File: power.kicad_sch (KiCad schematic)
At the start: 36 parts, among them J501 PJ-002AH-SMT-TR, Q501 DMG2307LQ, U501 LMR50410, U502 TLV1117-50, U503 TLV74133PDBVR

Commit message: Update some part numbers for in-stock parts
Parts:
- C501, C505, C511, C512: footprint Capacitor_SMD:CP_Elec_6.3x7.7 -> Capacitor_SMD:CP_Elec_6.3x5.8; PN EEEFK1E101XP -> EEEFK1E101SP
- D502: value TZMC12-GS08 -> TZMC10-GS08; PN TZMC12-GS08 -> TZMC10-GS08
- FB501, FB502, FB503: value 600R@100MHz -> 1000R@100MHz; PN BLM21SP601SN1 -> 2508051027Y1
- Q501: value DMG2307LQ -> SI2371EDS-T1-GE3; PN DMG2307LQ -> SI2371EDS-T1-GE3
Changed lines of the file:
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@@
       (effects (font (size 1.27 1.27)) (justify left))
     )
-    (property "Value" "TZMC12-GS08" (id 1) (at 88.9 36.8299 90)
+    (property "Value" "TZMC10-GS08" (id 1) (at 88.9 36.8299 90)
       (effects (font (size 1.27 1.27)) (justify left))
     )
@@
       (effects (font (size 1.27 1.27)) hide)
     )
-    (property "PN" "TZMC12-GS08" (id 4) (at 86.36 35.56 0)
+    (property "PN" "TZMC10-GS08" (id 4) (at 86.36 35.56 0)
       (effects (font (size 1.27 1.27)) hide)
     )
@@
       (effects (font (size 1.27 1.27)) (justify left))
     )
-    (property "Footprint" "Capacitor_SMD:CP_Elec_6.3x7.7" (id 2) (at 111.76 45.72 0)
-      (effects (font (size 1.27 1.27)) hide)
-    )
-    (property "Datasheet" "https://industrial.panasonic.com/cdbs/www-data/pdf/RDE0000/ABA0000C1181.pdf" (id 3) (at 111.76 45.72 0)
-      (effects (font (size 1.27 1.27)) hide)
-    )
-    (property "PN" "EEEFK1E101XP" (id 4) (at 111.76 45.72 0)
+    (property "Footprint" "Capacitor_SMD:CP_Elec_6.3x5.8" (id 2) (at 111.76 45.72 0)
+      (effects (font (size 1.27 1.27)) hide)
+    )
+    (property "Datasheet" "https://www.mouser.co.uk/datasheet/2/315/ABA0000C1251-1138508.pdf" (id 3) (at 111.76 45.72 0)
+      (effects (font (size 1.27 1.27)) hide)
+    )
+    (property "PN" "EEEFK1E101SP" (id 4) (at 111.76 45.72 0)
       (effects (font (size 1.27 1.27)) hide)
     )
@@
       (effects (font (size 1.27 1.27)) (justify left))
     )
-    (property "Footprint" "Capacitor_SMD:CP_Elec_6.3x7.7" (id 2) (at 119.38 105.41 0)
-      (effects (font (size 1.27 1.27)) hide)
-    )
-    (property "Datasheet" "https://industrial.panasonic.com/cdbs/www-data/pdf/RDE0000/ABA0000C1181.pdf" (id 3) (at 119.38 105.41 0)
-      (effects (font (size 1.27 1.27)) hide)
-    )
-    (property "PN" "EEEFK1E101XP" (id 4) (at 119.38 105.41 0)
+    (property "Footprint" "Capacitor_SMD:CP_Elec_6.3x5.8" (id 2) (at 119.38 105.41 0)
+      (effects (font (size 1.27 1.27)) hide)
+    )
+    (property "Datasheet" "https://www.mouser.co.uk/datasheet/2/315/ABA0000C1251-1138508.pdf" (id 3) (at 119.38 105.41 0)
+      (effects (font (size 1.27 1.27)) hide)
+    )
+    (property "PN" "EEEFK1E101SP" (id 4) (at 119.38 105.41 0)
       (effects (font (size 1.27 1.27)) hide)
     )
@@
       (effects (font (size 1.27 1.27)) (justify left))
     )
-    (property "Footprint" "Capacitor_SMD:CP_Elec_6.3x7.7" (id 2) (at 168.91 132.08 0)
-      (effects (font (size 1.27 1.27)) hide)
-    )
-    (property "Datasheet" "https://industrial.panasonic.com/cdbs/www-data/pdf/RDE0000/ABA0000C1181.pdf" (id 3) (at 168.91 132.08 0)
-      (effects (font (size 1.27 1.27)) hide)
-    )
-    (property "PN" "EEEFK1E101XP" (id 4) (at 168.91 132.08 0)
+    (property "Footprint" "Capacitor_SMD:CP_Elec_6.3x5.8" (id 2) (at 168.91 132.08 0)
+      (effects (font (size 1.27 1.27)) hide)
+    )
+    (property "Datasheet" "https://www.mouser.co.uk/datasheet/2/315/ABA0000C1251-1138508.pdf" (id 3) (at 168.91 132.08 0)
+      (effects (font (size 1.27 1.27)) hide)
+    )
+    (property "PN" "EEEFK1E101SP" (id 4) (at 168.91 132.08 0)
       (effects (font (size 1.27 1.27)) hide)
     )
@@
       (effects (font (size 1.27 1.27)) (justify left))
     )
-    (property "Footprint" "Capacitor_SMD:CP_Elec_6.3x7.7" (id 2) (at 210.82 105.41 0)
-      (effects (font (size 1.27 1.27)) hide)
-    )
-    (property "Datasheet" "https://industrial.panasonic.com/cdbs/www-data/pdf/RDE0000/ABA0000C1181.pdf" (id 3) (at 210.82 105.41 0)
-      (effects (font (size 1.27 1.27)) hide)
-    )
-    (property "PN" "EEEFK1E101XP" (id 4) (at 210.82 105.41 0)
+    (property "Footprint" "Capacitor_SMD:CP_Elec_6.3x5.8" (id 2) (at 210.82 105.41 0)
+      (effects (font (size 1.27 1.27)) hide)
+    )
+    (property "Datasheet" "https://www.mouser.co.uk/datasheet/2/315/ABA0000C1251-1138508.pdf" (id 3) (at 210.82 105.41 0)
+      (effects (font (size 1.27 1.27)) hide)
+    )
+    (property "PN" "EEEFK1E101SP" (id 4) (at 210.82 105.41 0)
       (effects (font (size 1.27 1.27)) hide)
     )
@@
     (in_bom yes) (on_board yes)
     (property "Reference" "FB501" (id 0) (at 71.12 95.5802 90))
-    (property "Value" "600R@100MHz" (id 1) (at 71.12 97.8916 90))
+    (property "Value" "1000R@100MHz" (id 1) (at 71.12 97.8916 90))
     (property "Footprint" "Resistor_SMD:R_0805_2012Metric_Pad1.20x1.40mm_HandSolder" (id 2) (at 71.12 99.822 90)
       (effects (font (size 1.27 1.27)) hide)
     )
-    (property "Datasheet" "~" (id 3) (at 71.12 101.6 0)
-      (effects (font (size 1.27 1.27)) hide)
-    )
-    (property "PN" "BLM21SP601SN1" (id 4) (at 71.12 101.6 0)
+    (property "Datasheet" "https://www.mouser.co.uk/datasheet/2/150/2508051027Y1-1511733.pdf" (id 3) (at 71.12 101.6 0)
+      (effects (font (size 1.27 1.27)) hide)
+    )
+    (property "PN" "2508051027Y1" (id 4) (at 71.12 101.6 0)
       (effects (font (size 1.27 1.27)) hide)
     )
@@
     (in_bom yes) (on_board yes)
     (property "Reference" "FB502" (id 0) (at 105.41 24.4602 90))
-    (property "Value" "600R@100MHz" (id 1) (at 105.41 26.7716 90))
+    (property "Value" "1000R@100MHz" (id 1) (at 105.41 26.7716 90))
     (property "Footprint" "Resistor_SMD:R_0805_2012Metric_Pad1.20x1.40mm_HandSolder" (id 2) (at 105.41 28.702 90)
       (effects (font (size 1.27 1.27)) hide)
     )
-    (property "Datasheet" "~" (id 3) (at 105.41 30.48 0)
-      (effects (font (size 1.27 1.27)) hide)
-    )
-    (property "PN" "BLM21SP601SN1" (id 4) (at 105.41 30.48 0)
+    (property "Datasheet" "https://www.mouser.co.uk/datasheet/2/150/2508051027Y1-1511733.pdf" (id 3) (at 105.41 30.48 0)
+      (effects (font (size 1.27 1.27)) hide)
+    )
+    (property "PN" "2508051027Y1" (id 4) (at 105.41 30.48 0)
       (effects (font (size 1.27 1.27)) hide)
     )
@@
     (in_bom yes) (on_board yes) (fields_autoplaced)
     (property "Reference" "FB503" (id 0) (at 143.51 95.25 90))
-    (property "Value" "600R@100MHz" (id 1) (at 143.51 97.79 90))
+    (property "Value" "1000R@100MHz" (id 1) (at 143.51 97.79 90))
     (property "Footprint" "Resistor_SMD:R_0805_2012Metric_Pad1.20x1.40mm_HandSolder" (id 2) (at 143.51 99.822 90)
       (effects (font (size 1.27 1.27)) hide)
     )
-    (property "Datasheet" "~" (id 3) (at 143.51 101.6 0)
-      (effects (font (size 1.27 1.27)) hide)
-    )
-    (property "PN" "BLM21SP601SN1" (id 4) (at 143.51 101.6 0)
+    (property "Datasheet" "https://www.mouser.co.uk/datasheet/2/150/2508051027Y1-1511733.pdf" (id 3) (at 143.51 101.6 0)
+      (effects (font (size 1.27 1.27)) hide)
+    )
+    (property "PN" "2508051027Y1" (id 4) (at 143.51 101.6 0)
       (effects (font (size 1.27 1.27)) hide)
     )
@@
     (in_bom yes) (on_board yes) (fields_autoplaced)
     (property "Reference" "Q501" (id 0) (at 78.74 22.86 90))
-    (property "Value" "DMG2307LQ" (id 1) (at 78.74 25.4 90))
+    (property "Value" "SI2371EDS-T1-GE3" (id 1) (at 78.74 25.4 90))
     (property "Footprint" "Package_TO_SOT_SMD:SOT-23" (id 2) (at 76.2 27.94 0)
       (effects (font (size 1.27 1.27)) hide)
     )
-    (property "Datasheet" "https://www.diodes.com/assets/Datasheets/DMG2307LQ.pdf" (id 3) (at 78.74 33.02 0)
-      (effects (font (size 1.27 1.27)) hide)
-    )
-    (property "PN" "DMG2307LQ" (id 4) (at 78.74 33.02 90)
-      (effects (font (size 1.27 1.27)) hide)
-    )
+    (property "Datasheet" "https://www.mouser.co.uk/datasheet/2/427/VISH_S_A0010613187_1-2571006.pdf" (id 3) (at 78.74 33.02 0)
+      (effects (font (size 1.27 1.27)) hide)
+    )
+    (property "PN" "SI2371EDS-T1-GE3" (id 4) (at 78.74 33.02 90)
+      (effects (font (size 1.27 1.27)) hide)
+    )

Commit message: WIP substitute parts
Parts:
- removed C506: 100n, Capacitor_SMD:C_0805_2012Metric_Pad1.18x1.45mm_HandSolder, symbol Device:C_Small
- removed R501: 1Meg, Resistor_SMD:R_0805_2012Metric_Pad1.20x1.40mm_HandSolder, symbol Device:R_Small
- removed R502: 200k, Resistor_SMD:R_0805_2012Metric_Pad1.20x1.40mm_HandSolder, symbol Device:R_Small
- removed U501: LMR50410, Package_TO_SOT_SMD:SOT-23-6_Handsoldering, symbol symbols:LMR50410
- added U?: LT1377CS8, Package_SO:SOIC-8_3.9x4.9mm_P1.27mm, symbol Regulator_Switching:LT1377CS8
- U503: value TLV74133PDBVR -> MIC5317-3.3YM5-TR; footprint Package_TO_SOT_SMD:SOT-23-5 -> Package_TO_SOT_SMD:SOT-23-5_HandSoldering; symbol symbols:TLV741xxPDBVR -> symbols:MIC5317-3.3YM5-TR; PN TLV74133PDBVR -> MIC5317-3.3YM5-TR
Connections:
- net +5V: no longer R506.2
- net +5V_F: now also R506.2
- net +6V: no longer L501.2
- net SW_FB: no longer names the net of R504.2, R505.1
- net SW_SW: no longer names the net of L501.1
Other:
- note added: "TODO redo this with https://www.ti.com/lit/ds/symlink/lmr12010.pdf"
- note added: "TPS5410MDREP"
- moved on the sheet: L501

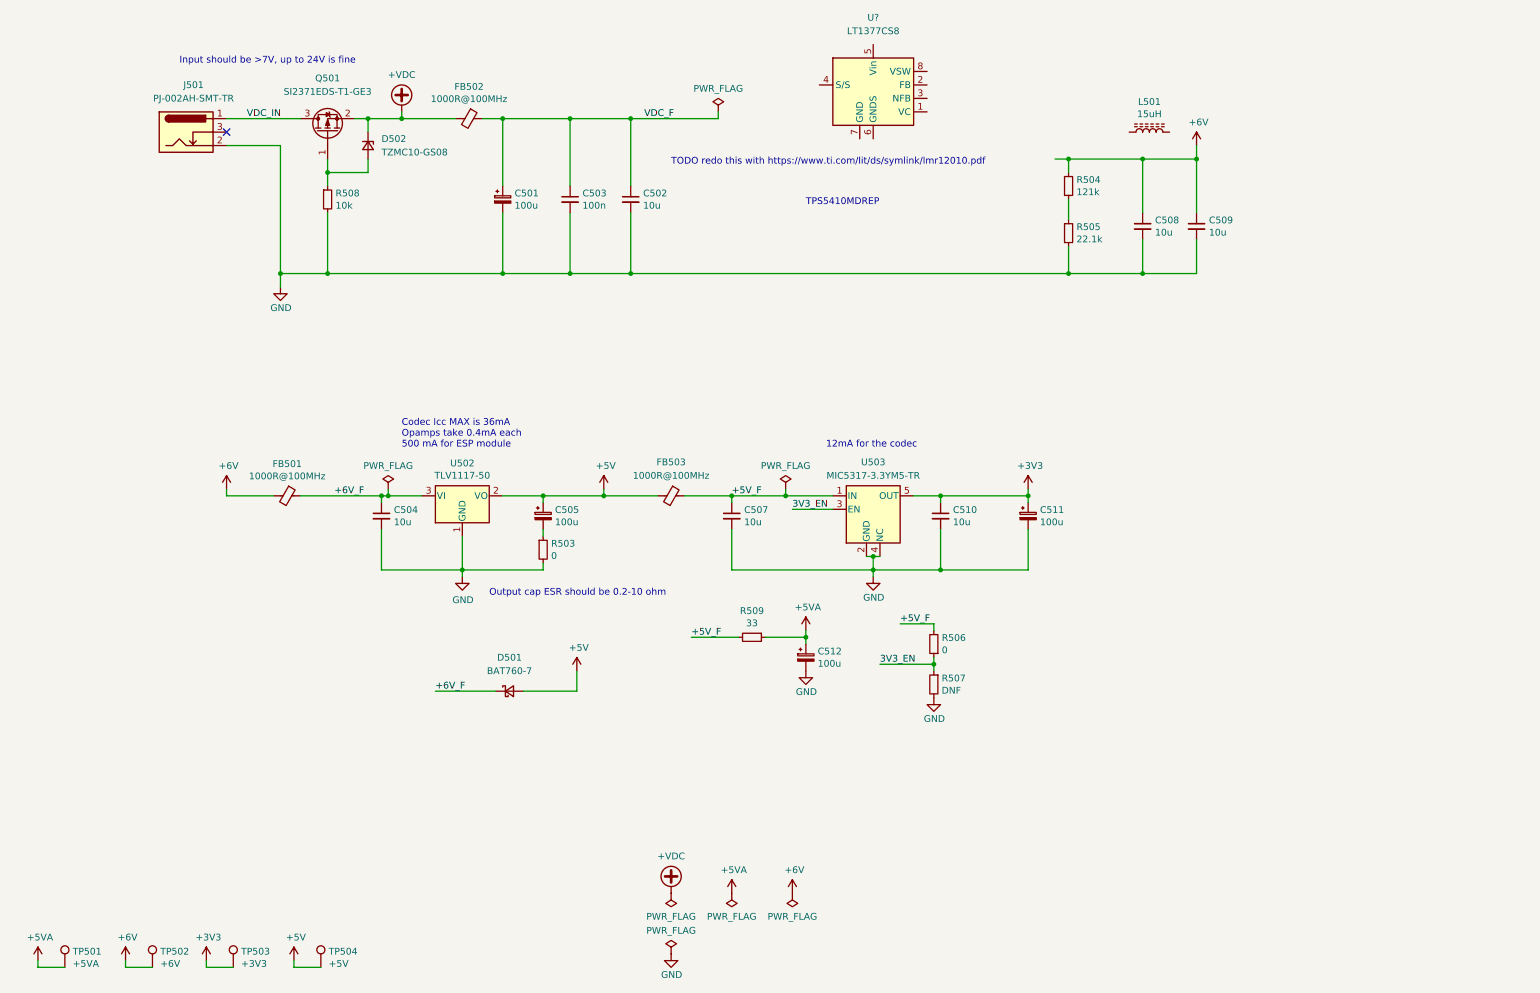
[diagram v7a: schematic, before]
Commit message: Add new switchmode power supply
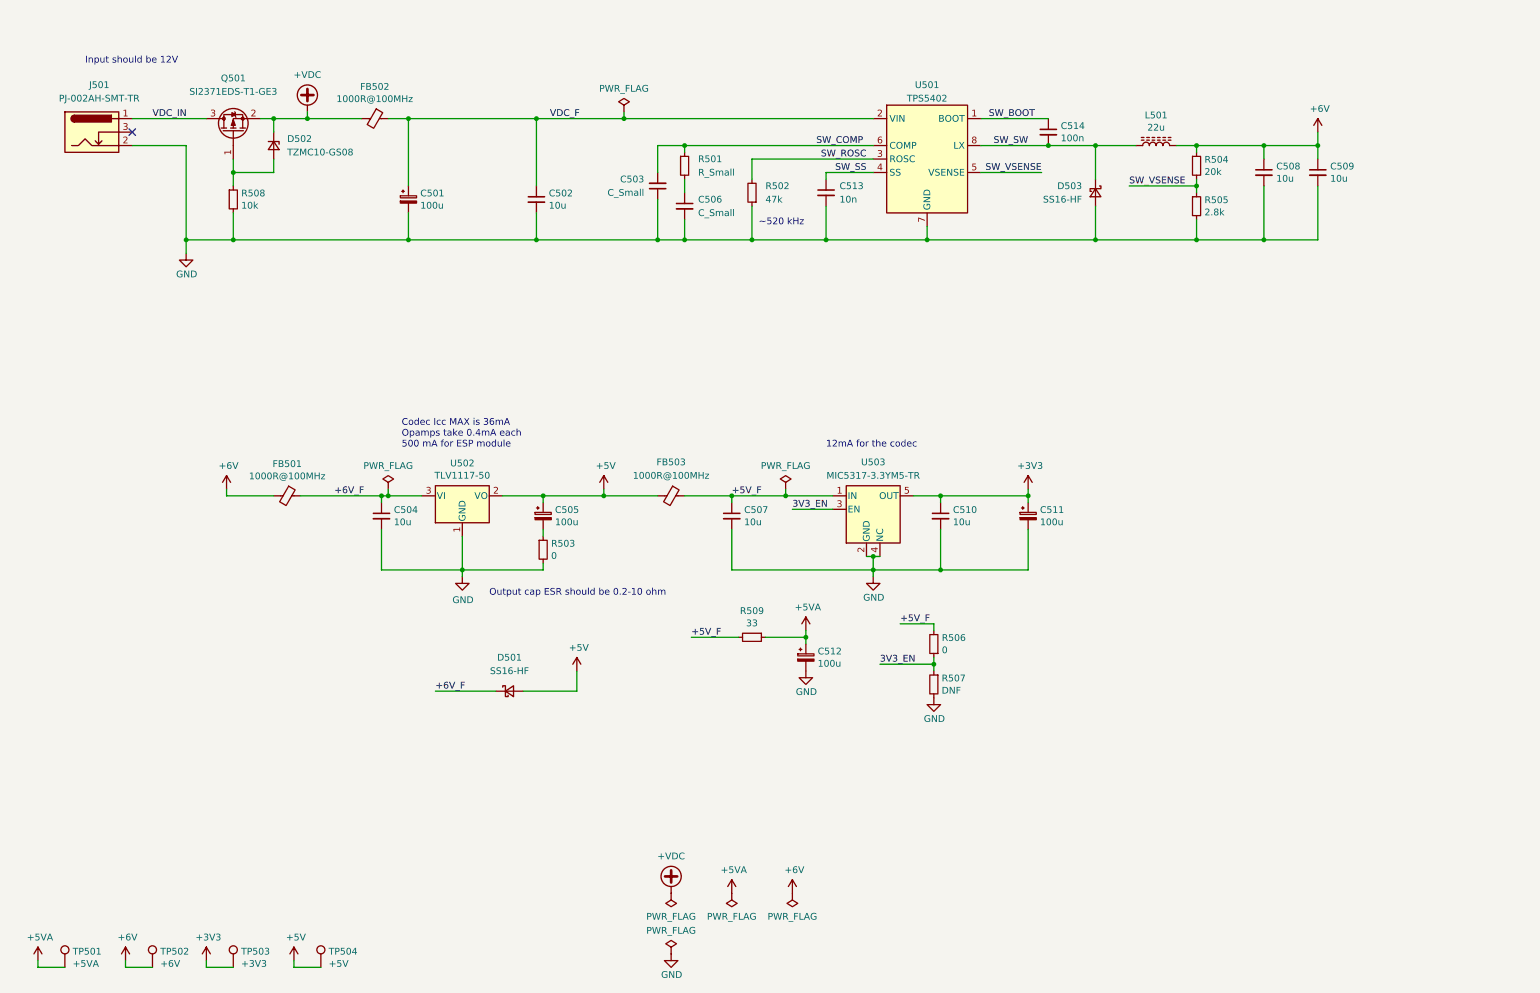
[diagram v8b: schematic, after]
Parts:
- removed U?: LT1377CS8, Package_SO:SOIC-8_3.9x4.9mm_P1.27mm, symbol Regulator_Switching:LT1377CS8
- added C506: C_Small, Capacitor_SMD:C_0805_2012Metric_Pad1.18x1.45mm_HandSolder, symbol Device:C_Small
- added C513: 10n, Capacitor_SMD:C_0805_2012Metric_Pad1.18x1.45mm_HandSolder, symbol Device:C_Small
- added C514: 100n, Capacitor_SMD:C_0805_2012Metric_Pad1.18x1.45mm_HandSolder, symbol Device:C_Small
- added D503: SS16-HF, Diode_SMD:D_SMA_Handsoldering, symbol Device:D_Schottky_Small
- added R501: R_Small, Resistor_SMD:R_0805_2012Metric_Pad1.20x1.40mm_HandSolder, symbol Device:R_Small
- added R502: 47k, Resistor_SMD:R_0805_2012Metric_Pad1.20x1.40mm_HandSolder, symbol Device:R_Small
- added U501: TPS5402, Package_SO:SOIC-8_3.9x4.9mm_P1.27mm, symbol symbols:TPS5402
- C502, C504, C507, C508, C509, C510: footprint Capacitor_SMD:C_1206_3216Metric_Pad1.33x1.80mm_HandSolder -> Capacitor_SMD:C_0805_2012Metric_Pad1.18x1.45mm_HandSolder; PN GMK316AB7106KL-TR -> GRM21BR61E106MA73L
- C503: value 100n -> C_Small; PN C0805C104M3RACTU -> (none)
- D501: value BAT760-7 -> SS16-HF; footprint Diode_SMD:D_SOD-323_HandSoldering -> Diode_SMD:D_SMA_Handsoldering; PN BAT760-7 -> SS16-HF
- L501: value 15uH -> 22u; footprint Inductor_SMD:L_Bourns-SRN8040_8x8.15mm -> (none); PN NRS8040T150MJGJ -> NRS5040T220MMGKV
- R504: value 121k -> 20k; PN CR0805-FX-1213ELF -> CR0805-FX-2002ELF
- R505: value 22.1k -> 2.8k; PN CR0805-FX-2212ELF -> CR0805-FX-2801ELF
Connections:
- net +6V: now also L501.2
- net GND: now also C503.1, C506.2, C513.2, D503.2 (A), R502.1, U501.7 (GND); no longer C503.2
- net VDC_F: now also U501.2 (VIN); no longer C503.1
- net SW_SW: now reaches L501.1
- net SW_SW: now also C514.2, D503.1 (K), U501.8 (LX)
- net SW_VSENSE: now reaches R504.2, R505.1
- net SW_VSENSE: now also U501.5 (VSENSE)
- new net: C506.1, R501.2
- new net SW_BOOT: C514.1, U501.1 (BOOT)
- new net SW_COMP: C503.2, R501.1, U501.6 (COMP)
- new net SW_ROSC: R502.2, U501.3 (ROSC)
- new net SW_SS: C513.1, U501.4 (SS)
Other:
- note added: "Input should be 12V"
- note added: "~520 kHz"
- note removed: "Input should be >7V, up to 24V is fine"
- note removed: "TODO redo this with https://www.ti.com/lit/ds/symlink/lmr12010.pdf"
- note removed: "TPS5410MDREP"
- moved on the sheet: C501, C502, C508, C509, D502, FB502, J501, L501, Q501, R504, R505, R508
